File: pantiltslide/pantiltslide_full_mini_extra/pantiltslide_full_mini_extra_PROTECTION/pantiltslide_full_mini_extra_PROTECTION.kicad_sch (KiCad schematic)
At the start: 81 parts, among them J1 Conn_01x22_Socket, J17 Motor_Slide, J18 Motor_Pan, J19 Motor_Tilt, J2 Conn_01x22_Socket, J20 TCA9548A_Mux, J21 AS5600_Pan, J22 AS5600_Tilt, J23 OLED, J24 TCA9548A_Mux, J26 Limit_Min, J27 Limit_Max, J28 Motor_Aux, J29 Enc_Slide, J3 MUX_2, J30 Enc_Pan, J31 Enc_Tilt, J32 Enc_Aux, J33 Btn_SetKeyframe, J34 Btn_ClearKeyframe, J35 Btn_PlayPause, J36 Btn_Reset, J37 5V_In, J38 24V_In, J4 MUX_3, J41 Aux_Max, J5 MUX_4, J6 MUX_5, J7 MUX_6, J8 MUX_7, U1 tmc2209, U2 tmc2209, U3 tmc2209, U4 tmc2209

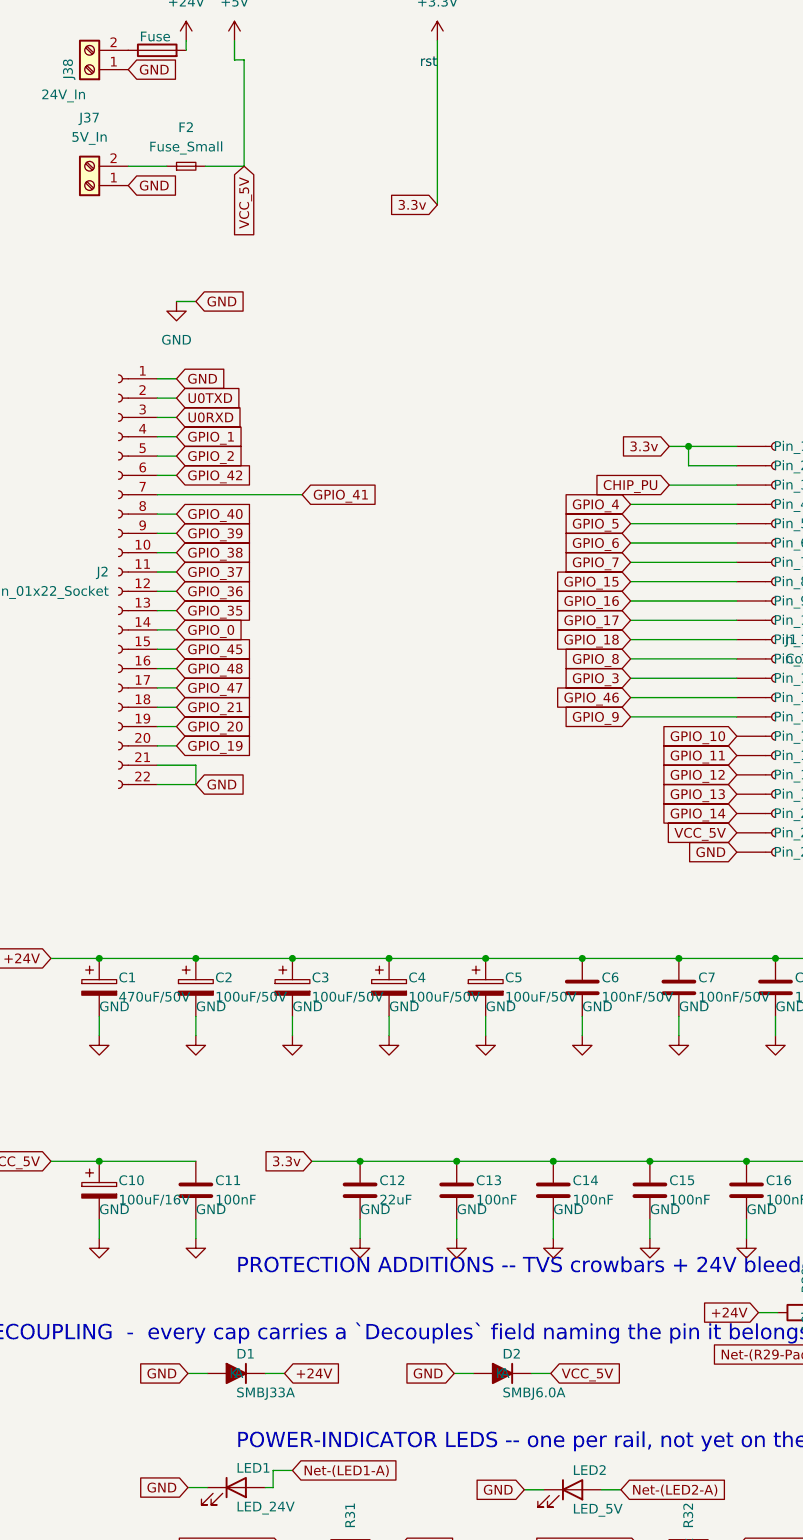
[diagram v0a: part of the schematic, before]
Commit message: mini_extra_PROTECTION: finalize BOM fields + layout cleanup
PCB layout (KiCad session):
- remove dangling 0.07mm VCC_5V stub near F2
- nudge F2/J37 to clear courtyard overlap
- fix J21 pad-2 GND thermal (was 1 spoke, now 2)
- zone refill; DRC now 0 errors / 0 unconnected

Schematic BOM fields:
- D1: LCSC C7427916 (NH), Manufacturer NH (was Brightking/C78419)
- D2: SMBJ6.5A, LCSC C52176732 (TDSEMIC), MPN/Mfr aligned (was SMBJ6.0A/LRC/C140903)
- F2: Value 1.5A, MPN 015401.5DR, Littelfuse, LCSC C206920
      (154 OMNI-BLOK 1.5A slow-blow Nano2 fuse+holder assembly)

Project:
- malformed_courtyard -> ignore (TMC2209 socket footprint has an
  open courtyard polygon; matches pantiltslide_full_turnkey_mini)

Still needs KiCad: Update PCB from Schematic (F8) to push the D1/D2/F2
MPN/Value/Notes fields into the board footprints (24 parity items ->
~8, remainder are the J3-J8 empty-footprint-field and REF** mounting
holes). Inner-layer copper In1 48% vs In2 55% (6.8pp) accepted -
board is only 93mm long, bow risk negligible.

Co-Authored-By: Claude Sonnet 5 <noreply@anthropic.com>
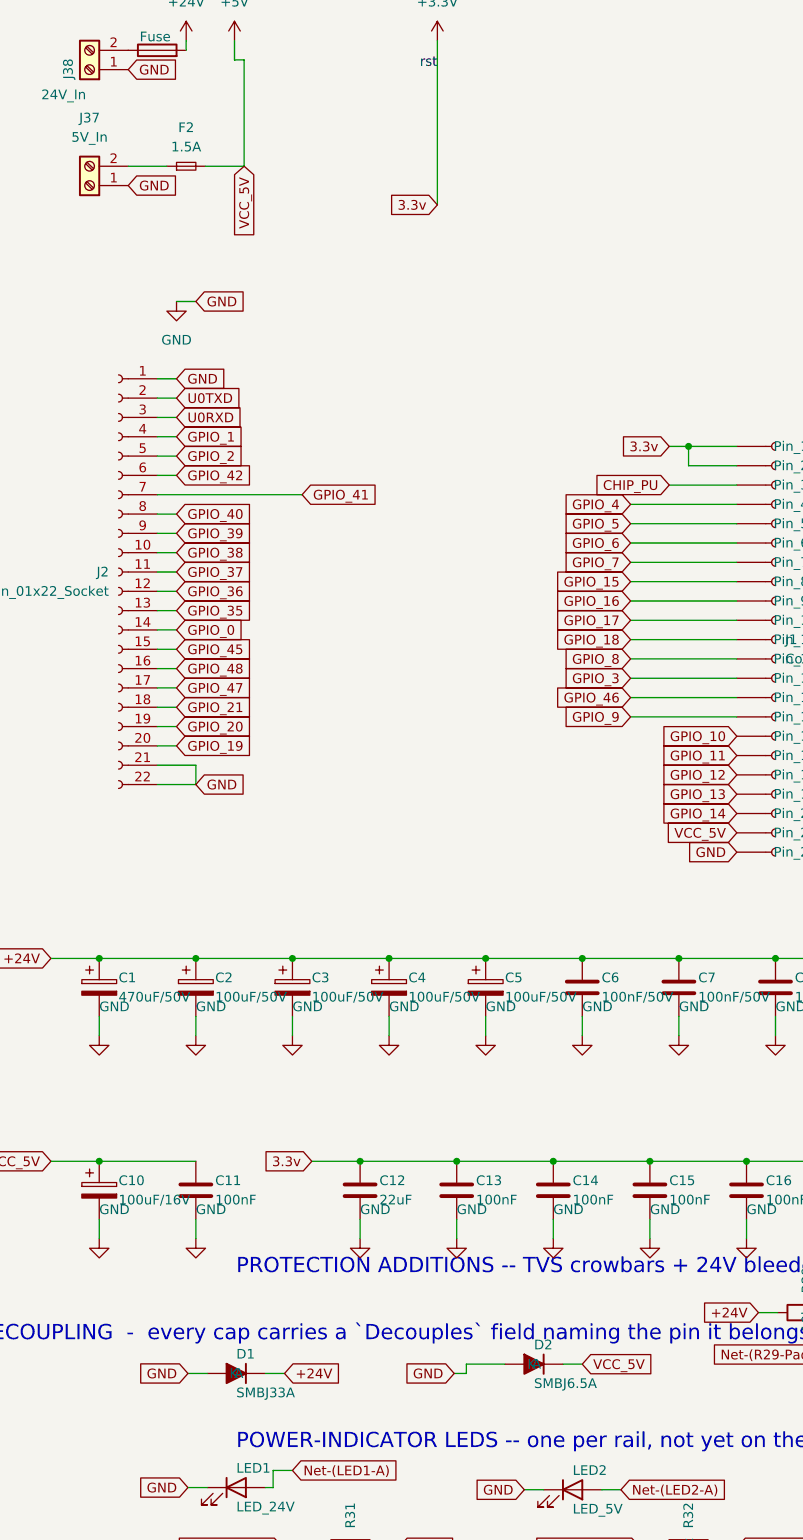
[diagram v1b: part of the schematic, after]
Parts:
- D1: LCSC C78419 -> C7427916; Manufacturer Brightking -> NH
- D2: value SMBJ6.0A -> SMBJ6.5A; LCSC C140903 -> C52176732; MPN SMBJ6.0A -> SMBJ6.5A; Manufacturer LRC -> TDSEMIC
- F2: value Fuse_Small -> 1.5A; LCSC (none) -> C206920; MPN (none) -> 015401.5DR; Manufacturer (none) -> Littelfuse; Notes (none) -> 154 Series OMNI-BLOK 1.5A slow-blow Nano2 fuse+holder assem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
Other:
- moved on the sheet: D2
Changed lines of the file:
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@@
 	(wire
 		(pts
+			(xy 95.25 199.39) (xy 95.25 200.61)
+		)
+		(stroke
+			(width 0)
+			(type default)
+		)
+	)
+	(wire
+		(pts
 			(xy 185.42 309.88) (xy 182.88 309.88)
 		)
@@
 	(wire
 		(pts
-			(xy 96.19 200.61) (xy 93.65 200.61)
+			(xy 100.33 199.39) (xy 95.25 199.39)
 		)
 		(stroke
@@
 	(wire
 		(pts
-			(xy 103.81 200.61) (xy 106.35 200.61)
+			(xy 107.95 199.39) (xy 110.49 199.39)
 		)
 		(stroke
@@
 	(wire
 		(pts
+			(xy 95.25 200.61) (xy 93.65 200.61)
+		)
+		(stroke
+			(width 0)
+			(type default)
+		)
+	)
+	(wire
+		(pts
 			(xy 279.4 266.7) (xy 271.78 266.7)
 		)
@@
 	(global_label "VCC_5V"
 		(shape input)
-		(at 106.35 200.61 0)
+		(at 110.49 199.39 0)
 		(effects
 			(font
@@
 		)
 		(property "Intersheetrefs" "${INTERSHEET_REFS}"
-			(at 106.35 200.61 0)
+			(at 110.49 199.39 0)
 			(hide yes)
 			(show_name no)
@@
 			)
 		)
-		(property "Value" "Fuse_Small"
+		(property "Value" "1.5A"
 			(at 58.42 39.37 0)
 			(show_name no)
@@
 			)
 		)
+		(property "MPN" "015401.5DR"
+			(at 58.42 41.91 0)
+			(hide yes)
+			(show_name no)
+			(do_not_autoplace no)
+			(effects
+				(font
+					(size 1.27 1.27)
+				)
+			)
+		)
+		(property "Manufacturer" "Littelfuse"
+			(at 58.42 41.91 0)
+			(hide yes)
+			(show_name no)
+			(do_not_autoplace no)
+			(effects
+				(font
+					(size 1.27 1.27)
+				)
+			)
+		)
+		(property "LCSC" "C206920"
+			(at 58.42 41.91 0)
+			(hide yes)
+			(show_name no)
+			(do_not_autoplace no)
+			(effects
+				(font
+					(size 1.27 1.27)
+				)
+			)
+		)
+		(property "Notes" "154 Series OMNI-BLOK 1.5A slow-blow Nano2 fuse+holder assembly, 125V, 50A breaking. VCC_5V fuse; downstream feeds D2 crowbar."
+			(at 58.42 41.91 0)
+			(hide yes)
+			(show_name no)
+			(do_not_autoplace no)
+			(effects
+				(font
+					(size 1.27 1.27)
+				)
+			)
+		)
 		(pin "1"
 		)
@@
 			)
 		)
-		(property "Manufacturer" "Brightking"
+		(property "Manufacturer" "NH"
 			(at 65 200.61 0)
 			(hide yes)
@@
 			)
 		)
-		(property "LCSC" "C78419"
+		(property "LCSC" "C7427916"
 			(at 65 200.61 0)
 			(hide yes)
@@
 	(symbol
 		(lib_id "Device:D")
-		(at 100 200.61 0)
+		(at 104.14 199.39 0)
 		(unit 1)
 		(body_style 1)
@@
 		(dnp no)
 		(property "Reference" "D2"
-			(at 100 198.07 0)
+			(at 104.14 196.85 0)
 			(show_name no)
 			(do_not_autoplace no)
@@
 			)
 		)
-		(property "Value" "SMBJ6.0A"
-			(at 100 203.15 0)
+		(property "Value" "SMBJ6.5A"
+			(at 104.14 201.93 0)
 			(show_name no)
 			(do_not_autoplace no)
@@
 		)
 		(property "Footprint" "Diode_SMD:D_SMB"
-			(at 100 200.61 0)
+			(at 104.14 199.39 0)
 			(hide yes)
 			(show_name no)
@@
 		)
 		(property "Datasheet" ""
-			(at 100 200.61 0)
+			(at 104.14 199.39 0)
 			(hide yes)
 			(show_name no)
@@
 		)
 		(property "Description" ""
-			(at 100 200.61 0)
+			(at 104.14 199.39 0)
 			(hide yes)
 			(show_name no)
@@
 			)
 		)
-		(property "MPN" "SMBJ6.0A"
-			(at 100 200.61 0)
+		(property "MPN" "SMBJ6.5A"
+			(at 104.14 199.39 0)
 			(hide yes)
 			(show_name no)
@@
 			)
 		)
-		(property "Manufacturer" "LRC"
-			(at 100 200.61 0)
+		(property "Manufacturer" "TDSEMIC"
+			(at 104.14 199.39 0)
 			(hide yes)
 			(show_name no)
@@
 			)
 		)
-		(property "LCSC" "C140903"
-			(at 100 200.61 0)
+		(property "LCSC" "C52176732"
+			(at 104.14 199.39 0)
 			(hide yes)
 			(show_name no)
@@
 		)
 		(property "Notes" "reverse-polarity crowbar + overvoltage clamp on VCC_5V"
-			(at 100 200.61 0)
+			(at 104.14 199.39 0)
 			(hide yes)
 			(show_name no)
